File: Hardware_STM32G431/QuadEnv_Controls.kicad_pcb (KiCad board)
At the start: 2 copper layers, 18.8 x 110 mm, 14 parts, among them J1 Conn_01x04_Male, J2 Conn_01x05_Male, J3 Conn_01x04_Male, J4 Conn_01x04_Male, J5 Gate_Out, J6 Env_Out

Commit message: First draft of Panel complete
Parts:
- moved RV1 1.00 mm to (59.4, 54.0)
- turned D1 to 90 degrees
- turned D2 to 180 degrees
- turned D3 to 0 degrees
- turned D4 to 90 degrees
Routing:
- net /Led1_Out: track 96.4 -> 99.0 mm
- net /Led4_Out: track 108.9 -> 111.4 mm
- net /Attack_Pot: track 22.0 -> 21.0 mm
- net /Led2_Out: track 99.1 -> 99.8 mm
- net /Led3_Out: track 114.6 -> 115.3 mm

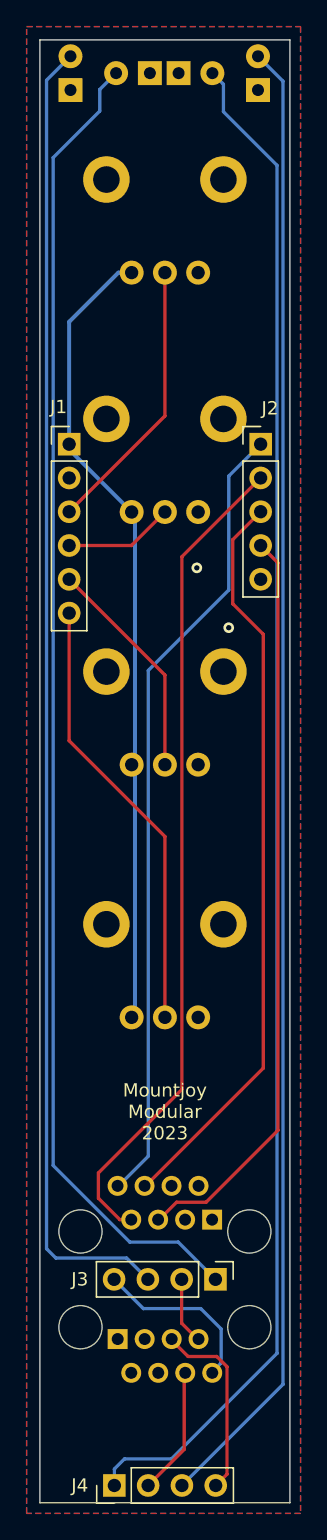
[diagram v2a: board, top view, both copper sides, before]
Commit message: Clean up project for manufacture
Fixed LED ordering bug on control board
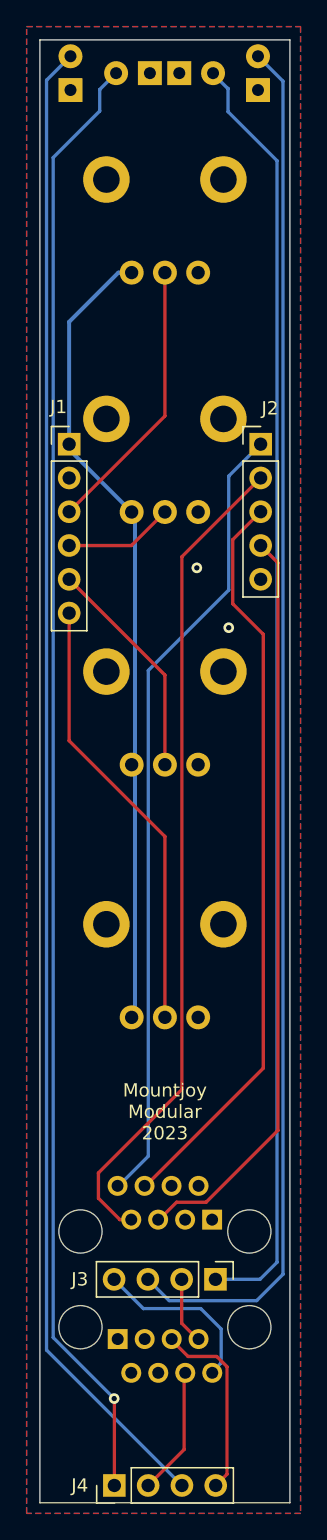
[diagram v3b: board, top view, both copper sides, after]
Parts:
- moved D1 14.1 mm to (66.4, 46.5)
- moved D4 14.1 mm to (52.3, 46.5)
- moved D2 4.75 mm to (61.8, 46.5), turned to 0 degrees
- moved D3 4.70 mm to (57.0, 46.5), turned to 180 degrees
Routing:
- net /Led3_Out: track 115.3 -> 110.1 mm, vias 0 -> 1
- net /Led1_Out: track 99.0 -> 104.0 mm
- net /Led2_Out: track 99.8 -> 96.6 mm
- net /Led4_Out: track 111.4 -> 112.4 mm
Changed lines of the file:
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@@
   )
   (footprint "Custom_Footprints:LED_D3.0mm" (layer "B.Cu")
-    (at 57 46.5 180)
+    (at 61.75 46.5)
     (descr "LED, diameter 3.0mm, 2 pins")
     (tags "LED diameter 3.0mm 2 pins")
@@
     (fp_arc (start -1.500555 -1.165476) (mid 1.9 -0.000452) (end -1.5 1.16619) (layer "B.Fab") (width 0.1))
     (fp_circle (center 0 0) (end 1.5 0) (layer "B.Fab") (width 0.1) (fill none))
-    (pad "1" thru_hole rect (at -1.27 0 180) (size 1.8 1.8) (drill 0.9) (layers *.Cu *.Mask)
+    (pad "1" thru_hole rect (at -1.27 0) (size 1.8 1.8) (drill 0.9) (layers *.Cu *.Mask)
       (net 1 "GND") (pinfunction "K") (pintype "passive"))
-    (pad "2" thru_hole circle (at 1.27 0 180) (size 1.8 1.8) (drill 0.9) (layers *.Cu *.Mask)
+    (pad "2" thru_hole circle (at 1.27 0) (size 1.8 1.8) (drill 0.9) (layers *.Cu *.Mask)
       (net 3 "/Led2_Out") (pinfunction "A") (pintype "passive"))
     (model "${KICAD6_3DMODEL_DIR}/LED_THT.3dshapes/LED_D3.0mm.wrl"
@@
   )
   (footprint "Custom_Footprints:LED_D3.0mm" (layer "B.Cu")
-    (at 52.3 46.5 90)
+    (at 66.4 46.5 90)
     (descr "LED, diameter 3.0mm, 2 pins")
     (tags "LED diameter 3.0mm 2 pins")
@@
   )
   (footprint "Custom_Footprints:LED_D3.0mm" (layer "B.Cu")
-    (at 66.4 46.5 90)
+    (at 52.3 46.5 90)
     (descr "LED, diameter 3.0mm, 2 pins")
     (tags "LED diameter 3.0mm 2 pins")
@@
   )
   (footprint "Custom_Footprints:LED_D3.0mm" (layer "B.Cu")
-    (at 61.7 46.5)
+    (at 57 46.5 180)
     (descr "LED, diameter 3.0mm, 2 pins")
     (tags "LED diameter 3.0mm 2 pins")
@@
     (fp_arc (start -1.500555 -1.165476) (mid 1.9 -0.000452) (end -1.5 1.16619) (layer "B.Fab") (width 0.1))
     (fp_circle (center 0 0) (end 1.5 0) (layer "B.Fab") (width 0.1) (fill none))
-    (pad "1" thru_hole rect (at -1.27 0) (size 1.8 1.8) (drill 0.9) (layers *.Cu *.Mask)
+    (pad "1" thru_hole rect (at -1.27 0 180) (size 1.8 1.8) (drill 0.9) (layers *.Cu *.Mask)
       (net 1 "GND") (pinfunction "K") (pintype "passive"))
-    (pad "2" thru_hole circle (at 1.27 0) (size 1.8 1.8) (drill 0.9) (layers *.Cu *.Mask)
+    (pad "2" thru_hole circle (at 1.27 0 180) (size 1.8 1.8) (drill 0.9) (layers *.Cu *.Mask)
       (net 4 "/Led3_Out") (pinfunction "A") (pintype "passive"))
     (model "${KICAD6_3DMODEL_DIR}/LED_THT.3dshapes/LED_D3.0mm.wrl"
@@
   (via (at 61.8 83.7) (size 0.8) (drill 0.4) (layers "F.Cu" "B.Cu") (free) (net 1))
   (via (at 64.2 88.2) (size 0.8) (drill 0.4) (layers "F.Cu" "B.Cu") (free) (net 1))
-  (segment (start 50.5 47.03) (end 52.3 45.23) (width 0.25) (layer "B.Cu") (net 2))
-  (segment (start 56.52 135.6) (end 51.2 135.6) (width 0.25) (layer "B.Cu") (net 2))
-  (segment (start 58.12 137.2) (end 56.52 135.6) (width 0.25) (layer "B.Cu") (net 2))
-  (segment (start 51.2 135.6) (end 50.5 134.9) (width 0.25) (layer "B.Cu") (net 2))
-  (segment (start 50.5 134.9) (end 50.5 47.03) (width 0.25) (layer "B.Cu") (net 2))
-  (segment (start 63.2 137.2) (end 60.4 134.4) (width 0.25) (layer "B.Cu") (net 3))
-  (segment (start 51 128.641571) (end 51 52.85) (width 0.25) (layer "B.Cu") (net 3))
-  (segment (start 54.5 49.35) (end 54.5 47.73) (width 0.25) (layer "B.Cu") (net 3))
-  (segment (start 60.4 134.4) (end 56.758429 134.4) (width 0.25) (layer "B.Cu") (net 3))
-  (segment (start 51 52.85) (end 54.5 49.35) (width 0.25) (layer "B.Cu") (net 3))
-  (segment (start 54.5 47.73) (end 55.73 46.5) (width 0.25) (layer "B.Cu") (net 3))
-  (segment (start 56.758429 134.4) (end 51 128.641571) (width 0.25) (layer "B.Cu") (net 3))
-  (segment (start 63.8 47.33) (end 62.97 46.5) (width 0.25) (layer "B.Cu") (net 4))
-  (segment (start 63.8 49.4) (end 63.8 47.33) (width 0.25) (layer "B.Cu") (net 4))
-  (segment (start 59.9 150.7) (end 67.830001 142.769999) (width 0.25) (layer "B.Cu") (net 4))
-  (segment (start 67.830001 142.769999) (end 67.830001 53.430001) (width 0.25) (layer "B.Cu") (net 4))
-  (segment (start 67.830001 53.430001) (end 63.8 49.4) (width 0.25) (layer "B.Cu") (net 4))
-  (segment (start 55.6 152.7) (end 55.6 151.46514) (width 0.25) (layer "B.Cu") (net 4))
-  (segment (start 55.6 151.46514) (end 56.36514 150.7) (width 0.25) (layer "B.Cu") (net 4))
-  (segment (start 56.36514 150.7) (end 59.9 150.7) (width 0.25) (layer "B.Cu") (net 4))
-  (segment (start 68.279502 145.100498) (end 68.279502 47.109502) (width 0.25) (layer "B.Cu") (net 5))
-  (segment (start 60.68 152.7) (end 68.279502 145.100498) (width 0.25) (layer "B.Cu") (net 5))
-  (segment (start 68.279502 47.109502) (end 66.4 45.23) (width 0.25) (layer "B.Cu") (net 5))
+  (segment (start 68.279502 136.820498) (end 68.279502 47.109502) (width 0.25) (layer "B.Cu") (net 2))
+  (segment (start 66.300001 138.799999) (end 59.719999 138.799999) (width 0.25) (layer "B.Cu") (net 2))
+  (segment (start 59.719999 138.799999) (end 58.12 137.2) (width 0.25) (layer "B.Cu") (net 2))
+  (segment (start 68.279502 136.820498) (end 66.300001 138.799999) (width 0.25) (layer "B.Cu") (net 2))
+  (segment (start 68.279502 47.109502) (end 66.4 45.23) (width 0.25) (layer "B.Cu") (net 2))
+  (segment (start 64.12 47.65) (end 62.97 46.5) (width 0.25) (layer "B.Cu") (net 3))
+  (segment (start 64.15 47.65) (end 64.12 47.65) (width 0.25) (layer "B.Cu") (net 3))
+  (segment (start 66.55 137.2) (end 67.830001 135.919999) (width 0.25) (layer "B.Cu") (net 3))
+  (segment (start 64.15 49.4) (end 64.15 47.65) (width 0.25) (layer "B.Cu") (net 3))
+  (segment (start 67.830001 53.080001) (end 64.15 49.4) (width 0.25) (layer "B.Cu") (net 3))
+  (segment (start 63.2 137.2) (end 66.55 137.2) (width 0.25) (layer "B.Cu") (net 3))
+  (segment (start 67.830001 135.919999) (end 67.830001 53.080001) (width 0.25) (layer "B.Cu") (net 3))
+  (segment (start 55.6 146.17843) (end 55.585785 146.164215) (width 0.25) (layer "F.Cu") (net 4))
+  (segment (start 55.6 152.7) (end 55.6 146.17843) (width 0.25) (layer "F.Cu") (net 4))
+  (via (at 55.585785 146.164215) (size 0.8) (drill 0.4) (layers "F.Cu" "B.Cu") (net 4))
+  (segment (start 54.5 49.35) (end 54.5 47.73) (width 0.25) (layer "B.Cu") (net 4))
+  (segment (start 51 141.578429) (end 55.585785 146.164215) (width 0.25) (layer "B.Cu") (net 4))
+  (segment (start 51 52.85) (end 54.5 49.35) (width 0.25) (layer "B.Cu") (net 4))
+  (segment (start 51 52.85) (end 51 141.578429) (width 0.25) (layer "B.Cu") (net 4))
+  (segment (start 54.5 47.73) (end 55.73 46.5) (width 0.25) (layer "B.Cu") (net 4))
+  (segment (start 52.3 45.23) (end 50.5 47.03) (width 0.25) (layer "B.Cu") (net 5))
+  (segment (start 50.5 47.03) (end 50.5 142.52) (width 0.25) (layer "B.Cu") (net 5))
+  (segment (start 50.5 142.52) (end 60.68 152.7) (width 0.25) (layer "B.Cu") (net 5))
   (segment (start 57.15 98.75) (end 56.9 98.5) (width 0.3) (layer "B.Cu") (net 6))
   (segment (start 56.9 79.5) (end 57.15 79.75) (width 0.3) (layer "B.Cu") (net 6))

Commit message: Corrections to schematic to fix sustain and release pots being switched
+Updated project to use production module parts and connections
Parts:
- RV3: value ReleasePot -> SustainPot
- RV4: value SustainPot -> ReleasePot
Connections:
- J1 pad 5: /Release_Pot -> /Sustain_Pot
- J1 pad 6: /Sustain_Pot -> /Release_Pot
- RV3 pad 2: /Release_Pot -> /Sustain_Pot
- RV4 pad 2: /Sustain_Pot -> /Release_Pot
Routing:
- net /Sustain_Pot: track 33.4 -> 16.9 mm
- net /Release_Pot: track 16.9 -> 33.4 mm
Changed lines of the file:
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@@
       (net 8 "/Decay_Pot") (pinfunction "Pin_4") (pintype "passive"))
     (pad "5" thru_hole oval locked (at 0 10.16) (size 1.7 1.7) (drill 1) (layers *.Cu *.Mask)
-      (net 9 "/Release_Pot") (pinfunction "Pin_5") (pintype "passive"))
+      (net 10 "/Sustain_Pot") (pinfunction "Pin_5") (pintype "passive"))
     (pad "6" thru_hole oval locked (at 0 12.7) (size 1.7 1.7) (drill 1) (layers *.Cu *.Mask)
-      (net 10 "/Sustain_Pot") (pinfunction "Pin_6") (pintype "passive"))
+      (net 9 "/Release_Pot") (pinfunction "Pin_6") (pintype "passive"))
     (model "${KICAD6_3DMODEL_DIR}/Connector_PinHeader_2.54mm.3dshapes/PinHeader_1x06_P2.54mm_Vertical.wrl"
       (offset (xyz 0 0 0))
@@
       (effects (font (size 1 1) (thickness 0.15)) (justify mirror))
     )
-    (fp_text value "SustainPot" (at 0 -9.8) (layer "B.SilkS")
+    (fp_text value "ReleasePot" (at 0 -9.8) (layer "B.SilkS")
       (effects (font (size 1 1) (thickness 0.15)) (justify mirror))
     )
@@
       (net 6 "+3.3VA") (pinfunction "1") (pintype "passive"))
     (pad "2" thru_hole circle (at 0 -7.5 90) (size 1.8 1.8) (drill 1) (layers *.Cu *.Mask)
-      (net 10 "/Sustain_Pot") (pinfunction "2") (pintype "passive"))
+      (net 9 "/Release_Pot") (pinfunction "2") (pintype "passive"))
     (pad "3" thru_hole circle (at -2.5 -7.5 90) (size 1.8 1.8) (drill 1) (layers *.Cu *.Mask)
       (net 1 "GND") (pinfunction "3") (pintype "passive"))
@@
       (effects (font (size 1 1) (thickness 0.15)) (justify mirror))
     )
-    (fp_text value "ReleasePot" (at 0 -9.7) (layer "B.SilkS")
+    (fp_text value "SustainPot" (at 0 -9.7) (layer "B.SilkS")
       (effects (font (size 1 1) (thickness 0.15)) (justify mirror))
     )
@@
       (net 6 "+3.3VA") (pinfunction "1") (pintype "passive"))
     (pad "2" thru_hole circle (at 0 -7.5 90) (size 1.8 1.8) (drill 1) (layers *.Cu *.Mask)
-      (net 9 "/Release_Pot") (pinfunction "2") (pintype "passive"))
+      (net 10 "/Sustain_Pot") (pinfunction "2") (pintype "passive"))
     (pad "3" thru_hole circle (at -2.5 -7.5 90) (size 1.8 1.8) (drill 1) (layers *.Cu *.Mask)
       (net 1 "GND") (pinfunction "3") (pintype "passive"))
@@
   (segment (start 56.88 82.02) (end 52.2 82.02) (width 0.25) (layer "F.Cu") (net 8))
   (segment (start 59.4 79.5) (end 56.88 82.02) (width 0.25) (layer "F.Cu") (net 8))
-  (segment (start 59.4 91.76) (end 52.2 84.56) (width 0.25) (layer "F.Cu") (net 9))
-  (segment (start 59.4 98.5) (end 59.4 91.76) (width 0.25) (layer "F.Cu") (net 9))
-  (segment (start 59.4 117.5) (end 59.4 103.9) (width 0.25) (layer "F.Cu") (net 10))
-  (segment (start 52.2 96.7) (end 52.2 87.1) (width 0.25) (layer "F.Cu") (net 10))
-  (segment (start 59.4 103.9) (end 52.2 96.7) (width 0.25) (layer "F.Cu") (net 10))
+  (segment (start 59.4 117.5) (end 59.4 103.9) (width 0.25) (layer "F.Cu") (net 9))
+  (segment (start 52.2 96.7) (end 52.2 87.1) (width 0.25) (layer "F.Cu") (net 9))
+  (segment (start 59.4 103.9) (end 52.2 96.7) (width 0.25) (layer "F.Cu") (net 9))
+  (segment (start 59.4 91.76) (end 52.2 84.56) (width 0.25) (layer "F.Cu") (net 10))
+  (segment (start 59.4 98.5) (end 59.4 91.76) (width 0.25) (layer "F.Cu") (net 10))
   (segment (start 60.66 140.5) (end 61.85 141.69) (width 0.25) (layer "F.Cu") (net 11))
   (segment (start 60.66 137.2) (end 60.66 140.5) (width 0.25) (layer "F.Cu") (net 11))
